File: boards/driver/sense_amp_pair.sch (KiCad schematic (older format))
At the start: 15 parts, among them T1 1:1, T2 1:1, U2 SN7524

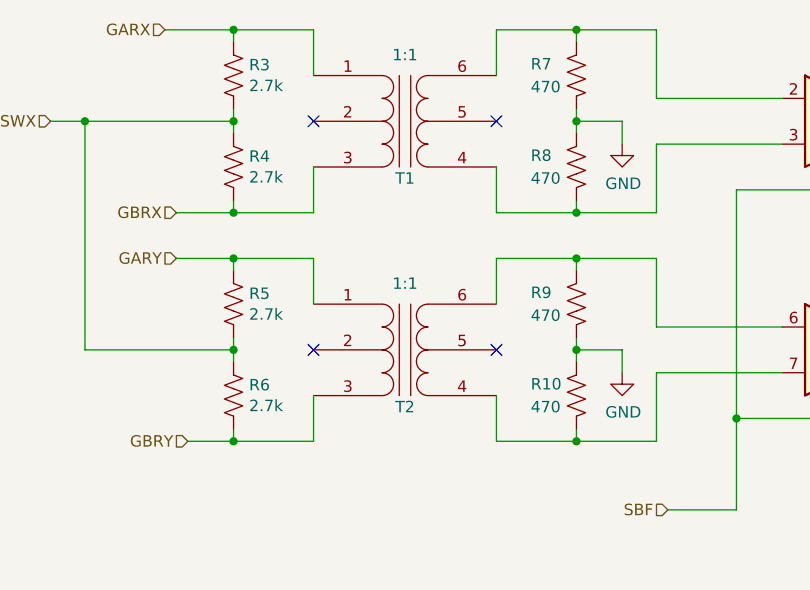
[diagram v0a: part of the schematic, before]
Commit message: Driver board: integrated DIN 41612 backplane connector, and made a dedicated parity inhibit sheet with a different set resistor value.
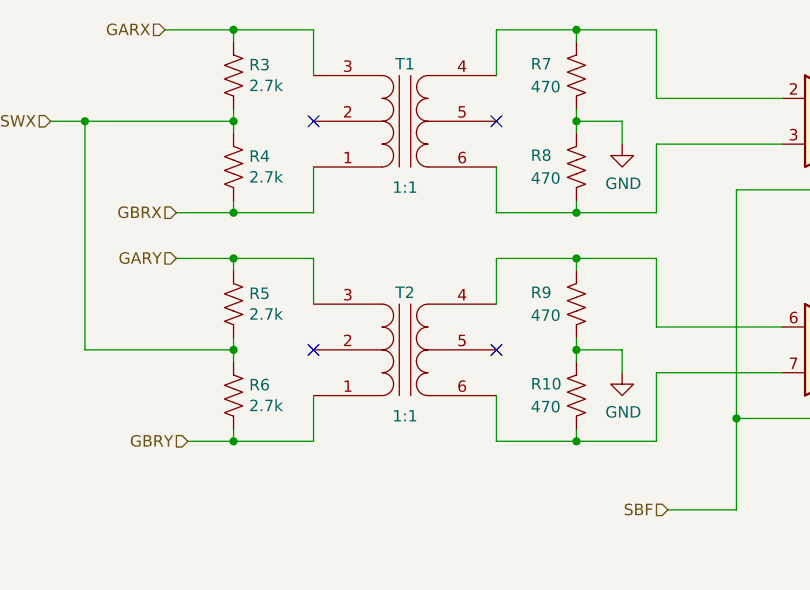
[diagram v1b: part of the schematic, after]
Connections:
- net GARX: now also T1.3 (P2); no longer T1.1 (P1)
- net GARY: now also T2.3 (P2); no longer T2.1 (P1)
- net GBRX: now also T1.1 (P1); no longer T1.3 (P2)
- net GBRY: now also T2.1 (P1); no longer T2.3 (P2)
- net at R7.1, U2.2: now also T1.4 (S2); no longer T1.6 (S1)
- net at R8.2, U2.3: now also T1.6 (S1); no longer T1.4 (S2)
- net at R9.1, U2.6: now also T2.4 (S2); no longer T2.6 (S1)
- net at R10.2, U2.7: now also T2.6 (S1); no longer T2.4 (S2)
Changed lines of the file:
@@
 F 3 "~" H 3650 2050 50  0001 C CNN
 	1    3650 2050
-	1    0    0    -1
+	1    0    0    1
 $EndComp
 NoConn ~ 3250 2050
@@
 F 3 "~" H 3650 3050 50  0001 C CNN
 	1    3650 3050
-	1    0    0    -1
+	1    0    0    1
 $EndComp
 NoConn ~ 3250 3050

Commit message: Driver: incorporated some power LEDs
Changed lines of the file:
@@
 AR Path="/61EC7443/638F119D/6358F0BC" Ref="R51"  Part="1"
 AR Path="/61EC7443/638F11C1/6358F0BC" Ref="R59"  Part="1"
-F 0 "R3" H 2968 1896 50  0000 L CNN
+F 0 "R59" H 2968 1896 50  0000 L CNN
 F 1 "2.7k" H 2968 1805 50  0000 L CNN
 F 2 "Resistor_SMD:R_0603_1608Metric" V 2940 1840 50  0001 C CNN
@@
 AR Path="/61EC7443/638F119D/6358F0C2" Ref="R52"  Part="1"
 AR Path="/61EC7443/638F11C1/6358F0C2" Ref="R60"  Part="1"
-F 0 "R4" H 2968 2296 50  0000 L CNN
+F 0 "R60" H 2968 2296 50  0000 L CNN
 F 1 "2.7k" H 2968 2205 50  0000 L CNN
 F 2 "Resistor_SMD:R_0603_1608Metric" V 2940 2240 50  0001 C CNN
@@
 AR Path="/61EC7443/638F119D/6358F0D6" Ref="R55"  Part="1"
 AR Path="/61EC7443/638F11C1/6358F0D6" Ref="R63"  Part="1"
-F 0 "R7" H 4600 1900 50  0000 R CNN
+F 0 "R63" H 4600 1900 50  0000 R CNN
 F 1 "470" H 4600 1800 50  0000 R CNN
 F 2 "Resistor_SMD:R_0603_1608Metric" V 4440 1840 50  0001 C CNN
@@
 AR Path="/61EC7443/638F119D/6358F0DC" Ref="R56"  Part="1"
 AR Path="/61EC7443/638F11C1/6358F0DC" Ref="R64"  Part="1"
-F 0 "R8" H 4600 2300 50  0000 R CNN
+F 0 "R64" H 4600 2300 50  0000 R CNN
 F 1 "470" H 4600 2200 50  0000 R CNN
 F 2 "Resistor_SMD:R_0603_1608Metric" V 4440 2240 50  0001 C CNN
@@
 AR Path="/61EC7443/638F119D/6358F0F0" Ref="#PWR043"  Part="1"
 AR Path="/61EC7443/638F11C1/6358F0F0" Ref="#PWR049"  Part="1"
-F 0 "#PWR07" H 4600 1900 50  0001 C CNN
+F 0 "#PWR049" H 4600 1900 50  0001 C CNN
 F 1 "GND" H 4605 1977 50  0000 C CNN
 F 2 "" H 4600 2150 50  0001 C CNN
@@
 AR Path="/61EC7443/638F119D/6358F0F7" Ref="U8"  Part="1"
 AR Path="/61EC7443/638F11C1/6358F0F7" Ref="U9"  Part="1"
-F 0 "U2" H 5600 2417 50  0000 C CNN
+F 0 "U9" H 5600 2417 50  0000 C CNN
 F 1 "SN7524" H 5600 2326 50  0000 C CNN
 F 2 "Package_DIP:DIP-16_W7.62mm_Socket" H 5600 2050 50  0001 C CNN
@@
 AR Path="/61EC7443/638F119D/6358F101" Ref="T13"  Part="1"
 AR Path="/61EC7443/638F11C1/6358F101" Ref="T15"  Part="1"
-F 0 "T1" H 3650 1800 50  0000 C CNN
+F 0 "T15" H 3650 1800 50  0000 C CNN
 F 1 "1:1" H 3650 2340 50  0000 C CNN
 F 2 "lachesis:Transformer_Murata_786J" H 3650 2050 50  0001 C CNN
@@
 AR Path="/61EC7443/638F119D/6358F10F" Ref="R53"  Part="1"
 AR Path="/61EC7443/638F11C1/6358F10F" Ref="R61"  Part="1"
-F 0 "R5" H 2968 2896 50  0000 L CNN
+F 0 "R61" H 2968 2896 50  0000 L CNN
 F 1 "2.7k" H 2968 2805 50  0000 L CNN
 F 2 "Resistor_SMD:R_0603_1608Metric" V 2940 2840 50  0001 C CNN
@@
 AR Path="/61EC7443/638F119D/6358F115" Ref="R54"  Part="1"
 AR Path="/61EC7443/638F11C1/6358F115" Ref="R62"  Part="1"
-F 0 "R6" H 2968 3296 50  0000 L CNN
+F 0 "R62" H 2968 3296 50  0000 L CNN
 F 1 "2.7k" H 2968 3205 50  0000 L CNN
 F 2 "Resistor_SMD:R_0603_1608Metric" V 2940 3240 50  0001 C CNN
@@
 AR Path="/61EC7443/638F119D/6358F125" Ref="R57"  Part="1"
 AR Path="/61EC7443/638F11C1/6358F125" Ref="R65"  Part="1"
-F 0 "R9" H 4600 2900 50  0000 R CNN
+F 0 "R65" H 4600 2900 50  0000 R CNN
 F 1 "470" H 4600 2800 50  0000 R CNN
 F 2 "Resistor_SMD:R_0603_1608Metric" V 4440 2840 50  0001 C CNN
@@
 AR Path="/61EC7443/638F119D/6358F12B" Ref="R58"  Part="1"
 AR Path="/61EC7443/638F11C1/6358F12B" Ref="R66"  Part="1"
-F 0 "R10" H 4600 3300 50  0000 R CNN
+F 0 "R66" H 4600 3300 50  0000 R CNN
 F 1 "470" H 4600 3200 50  0000 R CNN
 F 2 "Resistor_SMD:R_0603_1608Metric" V 4440 3240 50  0001 C CNN
@@
 AR Path="/61EC7443/638F119D/6358F13F" Ref="#PWR044"  Part="1"
 AR Path="/61EC7443/638F11C1/6358F13F" Ref="#PWR050"  Part="1"
-F 0 "#PWR08" H 4600 2900 50  0001 C CNN
+F 0 "#PWR050" H 4600 2900 50  0001 C CNN
 F 1 "GND" H 4605 2977 50  0000 C CNN
 F 2 "" H 4600 3150 50  0001 C CNN
@@
 AR Path="/61EC7443/638F119D/6358F146" Ref="U8"  Part="2"
 AR Path="/61EC7443/638F11C1/6358F146" Ref="U9"  Part="2"
-F 0 "U2" H 5600 3417 50  0000 C CNN
+F 0 "U9" H 5600 3417 50  0000 C CNN
 F 1 "SN7524" H 5600 3326 50  0000 C CNN
 F 2 "Package_DIP:DIP-16_W7.62mm_Socket" H 5600 3050 50  0001 C CNN
@@
 AR Path="/61EC7443/638F119D/6358F150" Ref="T14"  Part="1"
 AR Path="/61EC7443/638F11C1/6358F150" Ref="T16"  Part="1"
-F 0 "T2" H 3650 2800 50  0000 C CNN
+F 0 "T16" H 3650 2800 50  0000 C CNN
 F 1 "1:1" H 3650 3340 50  0000 C CNN
 F 2 "lachesis:Transformer_Murata_786J" H 3650 3050 50  0001 C CNN
@@
 AR Path="/61EC7443/638F119D/6359BB32" Ref="U8"  Part="4"
 AR Path="/61EC7443/638F11C1/6359BB32" Ref="U9"  Part="4"
-F 0 "U2" H 8050 3050 50  0000 L CNN
+F 0 "U9" H 8050 3050 50  0000 L CNN
 F 1 "SN7524" H 8050 2950 50  0000 L CNN
 F 2 "Package_DIP:DIP-16_W7.62mm_Socket" H 8100 3350 50  0001 C CNN
@@
 AR Path="/61EC7443/638F119D/6359BB38" Ref="#PWR048"  Part="1"
 AR Path="/61EC7443/638F11C1/6359BB38" Ref="#PWR054"  Part="1"
-F 0 "#PWR012" H 8550 3300 50  0001 C CNN
+F 0 "#PWR054" H 8550 3300 50  0001 C CNN
 F 1 "GND" H 8555 3377 50  0000 C CNN
 F 2 "" H 8550 3550 50  0001 C CNN
@@
 AR Path="/61EC7443/638F119D/6359BB40" Ref="C29"  Part="1"
 AR Path="/61EC7443/638F11C1/6359BB40" Ref="C33"  Part="1"
-F 0 "C5" H 8459 3304 50  0000 R CNN
+F 0 "C33" H 8459 3304 50  0000 R CNN
 F 1 "100pF" H 8459 3395 50  0000 R CNN
 F 2 "Capacitor_SMD:C_0603_1608Metric" H 8550 3350 50  0001 C CNN
@@
 AR Path="/61EC7443/638F119D/635A5721" Ref="C30"  Part="1"
 AR Path="/61EC7443/638F11C1/635A5721" Ref="C34"  Part="1"
-F 0 "C6" H 8808 3154 50  0000 R CNN
+F 0 "C34" H 8808 3154 50  0000 R CNN
 F 1 "0.1uF" H 8808 3245 50  0000 R CNN
 F 2 "Capacitor_SMD:C_0603_1608Metric" H 8900 3200 50  0001 C CNN
@@
 AR Path="/61EC7443/638F119D/635A572B" Ref="C31"  Part="1"
 AR Path="/61EC7443/638F11C1/635A572B" Ref="C35"  Part="1"
-F 0 "C7" H 8808 3654 50  0000 R CNN
+F 0 "C35" H 8808 3654 50  0000 R CNN
 F 1 "0.1uF" H 8808 3745 50  0000 R CNN
 F 2 "Capacitor_SMD:C_0603_1608Metric" H 8900 3700 50  0001 C CNN
@@
 AR Path="/61EC7443/638F119D/635B04D5" Ref="U8"  Part="3"
 AR Path="/61EC7443/638F11C1/635B04D5" Ref="U9"  Part="3"
-F 0 "U2" H 5750 4350 50  0000 C CNN
+F 0 "U9" H 5750 4350 50  0000 C CNN
 F 1 "SN7524" H 5700 4250 50  0000 C CNN
 F 2 "Package_DIP:DIP-16_W7.62mm_Socket" H 5550 4450 50  0001 C CNN
@@
 AR Path="/61EC7443/638F119D/635B04DD" Ref="C28"  Part="1"
 AR Path="/61EC7443/638F11C1/635B04DD" Ref="C32"  Part="1"
-F 0 "C4" H 5009 4404 50  0000 R CNN
+F 0 "C32" H 5009 4404 50  0000 R CNN
 F 1 "10nF" H 5009 4495 50  0000 R CNN
 F 2 "Capacitor_SMD:C_0603_1608Metric" H 5100 4450 50  0001 C CNN
@@
 AR Path="/61EC7443/638F119D/635B04EA" Ref="#PWR045"  Part="1"
 AR Path="/61EC7443/638F11C1/635B04EA" Ref="#PWR051"  Part="1"
-F 0 "#PWR09" H 4750 4400 50  0001 C CNN
+F 0 "#PWR051" H 4750 4400 50  0001 C CNN
 F 1 "GND" H 4755 4477 50  0000 C CNN
 F 2 "" H 4750 4650 50  0001 C CNN
@@
 AR Path="/61EC7443/638F119D/635E31A4" Ref="#PWR046"  Part="1"
 AR Path="/61EC7443/638F11C1/635E31A4" Ref="#PWR052"  Part="1"
-F 0 "#PWR010" H 8000 2700 50  0001 C CNN
+F 0 "#PWR052" H 8000 2700 50  0001 C CNN
 F 1 "+5V" H 8015 3023 50  0000 C CNN
 F 2 "" H 8000 2850 50  0001 C CNN
@@
 AR Path="/61EC7443/638F119D/635F8271" Ref="#PWR047"  Part="1"
 AR Path="/61EC7443/638F11C1/635F8271" Ref="#PWR053"  Part="1"
-F 0 "#PWR011" H 8000 4050 50  0001 C CNN
+F 0 "#PWR053" H 8000 4050 50  0001 C CNN
 F 1 "-5V" H 8015 4123 50  0000 C CNN
 F 2 "" H 8000 3950 50  0001 C CNN

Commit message: Driver board: largely fleshed out part selection
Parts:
- C4: Digikey (none) -> https://www.digikey.com/en/products/detail/samsung-electro-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; Part Number (none) -> CL10B103KC8NNNC; Rating (none) -> 100V; Tolerance (none) -> 10%
- C5: Digikey (none) -> https://www.digikey.com/en/products/detail/samsung-electro-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; Part Number (none) -> CL10B101KB8NFNC; Rating (none) -> 50V; Tolerance (none) -> 10%
- T1, T2: Digikey (none) -> https://www.digikey.com/en/products/detail/murata-power-sol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; Part Number (none) -> 78615/1JC
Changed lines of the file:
@@
 $Descr A4 11693 8268
 encoding utf-8
-Sheet 4 64
+Sheet 8 64
 Title ""
 Date ""
@@
 AR Path="/61EC7443/638F119D/6358F0BC" Ref="R51"  Part="1"
 AR Path="/61EC7443/638F11C1/6358F0BC" Ref="R59"  Part="1"
-F 0 "R59" H 2968 1896 50  0000 L CNN
+F 0 "R35" H 2968 1896 50  0000 L CNN
 F 1 "2.7k" H 2968 1805 50  0000 L CNN
 F 2 "Resistor_SMD:R_0603_1608Metric" V 2940 1840 50  0001 C CNN
@@
 AR Path="/61EC7443/638F119D/6358F0C2" Ref="R52"  Part="1"
 AR Path="/61EC7443/638F11C1/6358F0C2" Ref="R60"  Part="1"
-F 0 "R60" H 2968 2296 50  0000 L CNN
+F 0 "R36" H 2968 2296 50  0000 L CNN
 F 1 "2.7k" H 2968 2205 50  0000 L CNN
 F 2 "Resistor_SMD:R_0603_1608Metric" V 2940 2240 50  0001 C CNN
@@
 AR Path="/61EC7443/638F119D/6358F0D6" Ref="R55"  Part="1"
 AR Path="/61EC7443/638F11C1/6358F0D6" Ref="R63"  Part="1"
-F 0 "R63" H 4600 1900 50  0000 R CNN
+F 0 "R39" H 4600 1900 50  0000 R CNN
 F 1 "470" H 4600 1800 50  0000 R CNN
 F 2 "Resistor_SMD:R_0603_1608Metric" V 4440 1840 50  0001 C CNN
@@
 AR Path="/61EC7443/638F119D/6358F0DC" Ref="R56"  Part="1"
 AR Path="/61EC7443/638F11C1/6358F0DC" Ref="R64"  Part="1"
-F 0 "R64" H 4600 2300 50  0000 R CNN
+F 0 "R40" H 4600 2300 50  0000 R CNN
 F 1 "470" H 4600 2200 50  0000 R CNN
 F 2 "Resistor_SMD:R_0603_1608Metric" V 4440 2240 50  0001 C CNN
@@
 AR Path="/61EC7443/638F119D/6358F0F7" Ref="U8"  Part="1"
 AR Path="/61EC7443/638F11C1/6358F0F7" Ref="U9"  Part="1"
-F 0 "U9" H 5600 2417 50  0000 C CNN
+F 0 "U6" H 5600 2417 50  0000 C CNN
 F 1 "SN7524" H 5600 2326 50  0000 C CNN
 F 2 "Package_DIP:DIP-16_W7.62mm_Socket" H 5600 2050 50  0001 C CNN
@@
 AR Path="/61EC7443/638F119D/6358F101" Ref="T13"  Part="1"
 AR Path="/61EC7443/638F11C1/6358F101" Ref="T15"  Part="1"
-F 0 "T15" H 3650 1800 50  0000 C CNN
+F 0 "T9" H 3650 1800 50  0000 C CNN
 F 1 "1:1" H 3650 2340 50  0000 C CNN
 F 2 "lachesis:Transformer_Murata_786J" H 3650 2050 50  0001 C CNN
 F 3 "~" H 3650 2050 50  0001 C CNN
+F 4 "https://www.digikey.com/en/products/detail/murata-power-solutions-inc/78615-1JC/5798694" H 3650 2050 50  0001 C CNN "Digikey"
+F 5 "78615/1JC" H 3650 2050 50  0001 C CNN "Part Number"
 	1    3650 2050
 	1    0    0    1
@@
 AR Path="/61EC7443/638F119D/6358F10F" Ref="R53"  Part="1"
 AR Path="/61EC7443/638F11C1/6358F10F" Ref="R61"  Part="1"
-F 0 "R61" H 2968 2896 50  0000 L CNN
+F 0 "R37" H 2968 2896 50  0000 L CNN
 F 1 "2.7k" H 2968 2805 50  0000 L CNN
 F 2 "Resistor_SMD:R_0603_1608Metric" V 2940 2840 50  0001 C CNN
@@
 AR Path="/61EC7443/638F119D/6358F115" Ref="R54"  Part="1"
 AR Path="/61EC7443/638F11C1/6358F115" Ref="R62"  Part="1"
-F 0 "R62" H 2968 3296 50  0000 L CNN
+F 0 "R38" H 2968 3296 50  0000 L CNN
 F 1 "2.7k" H 2968 3205 50  0000 L CNN
 F 2 "Resistor_SMD:R_0603_1608Metric" V 2940 3240 50  0001 C CNN
@@
 AR Path="/61EC7443/638F119D/6358F125" Ref="R57"  Part="1"
 AR Path="/61EC7443/638F11C1/6358F125" Ref="R65"  Part="1"
-F 0 "R65" H 4600 2900 50  0000 R CNN
+F 0 "R41" H 4600 2900 50  0000 R CNN
 F 1 "470" H 4600 2800 50  0000 R CNN
 F 2 "Resistor_SMD:R_0603_1608Metric" V 4440 2840 50  0001 C CNN
@@
 AR Path="/61EC7443/638F119D/6358F12B" Ref="R58"  Part="1"
 AR Path="/61EC7443/638F11C1/6358F12B" Ref="R66"  Part="1"
-F 0 "R66" H 4600 3300 50  0000 R CNN
+F 0 "R42" H 4600 3300 50  0000 R CNN
 F 1 "470" H 4600 3200 50  0000 R CNN
 F 2 "Resistor_SMD:R_0603_1608Metric" V 4440 3240 50  0001 C CNN
@@
 AR Path="/61EC7443/638F119D/6358F146" Ref="U8"  Part="2"
 AR Path="/61EC7443/638F11C1/6358F146" Ref="U9"  Part="2"
-F 0 "U9" H 5600 3417 50  0000 C CNN
+F 0 "U6" H 5600 3417 50  0000 C CNN
 F 1 "SN7524" H 5600 3326 50  0000 C CNN
 F 2 "Package_DIP:DIP-16_W7.62mm_Socket" H 5600 3050 50  0001 C CNN
@@
 AR Path="/61EC7443/638F119D/6358F150" Ref="T14"  Part="1"
 AR Path="/61EC7443/638F11C1/6358F150" Ref="T16"  Part="1"
-F 0 "T16" H 3650 2800 50  0000 C CNN
+F 0 "T10" H 3650 2800 50  0000 C CNN
 F 1 "1:1" H 3650 3340 50  0000 C CNN
 F 2 "lachesis:Transformer_Murata_786J" H 3650 3050 50  0001 C CNN
 F 3 "~" H 3650 3050 50  0001 C CNN
+F 4 "https://www.digikey.com/en/products/detail/murata-power-solutions-inc/78615-1JC/5798694" H 3650 3050 50  0001 C CNN "Digikey"
+F 5 "78615/1JC" H 3650 3050 50  0001 C CNN "Part Number"
 	1    3650 3050
 	1    0    0    1
@@
 AR Path="/61EC7443/638F119D/6359BB32" Ref="U8"  Part="4"
 AR Path="/61EC7443/638F11C1/6359BB32" Ref="U9"  Part="4"
-F 0 "U9" H 8050 3050 50  0000 L CNN
+F 0 "U6" H 8050 3050 50  0000 L CNN
 F 1 "SN7524" H 8050 2950 50  0000 L CNN
 F 2 "Package_DIP:DIP-16_W7.62mm_Socket" H 8100 3350 50  0001 C CNN
@@
 AR Path="/61EC7443/638F119D/6359BB40" Ref="C29"  Part="1"
 AR Path="/61EC7443/638F11C1/6359BB40" Ref="C33"  Part="1"
-F 0 "C33" H 8459 3304 50  0000 R CNN
+F 0 "C21" H 8459 3304 50  0000 R CNN
 F 1 "100pF" H 8459 3395 50  0000 R CNN
 F 2 "Capacitor_SMD:C_0603_1608Metric" H 8550 3350 50  0001 C CNN
 F 3 "~" H 8550 3350 50  0001 C CNN
+F 4 "https://www.digikey.com/en/products/detail/samsung-electro-mechanics/CL10B101KB8NFNC/3887566" H 8550 3350 50  0001 C CNN "Digikey"
+F 5 "CL10B101KB8NFNC" H 8550 3350 50  0001 C CNN "Part Number"
+F 6 "50V" H 8550 3350 50  0001 C CNN "Rating"
+F 7 "10%" H 8550 3350 50  0001 C CNN "Tolerance"
 	1    8550 3350
 	-1   0    0    1
@@
 AR Path="/61EC7443/638F119D/635A5721" Ref="C30"  Part="1"
 AR Path="/61EC7443/638F11C1/635A5721" Ref="C34"  Part="1"
-F 0 "C34" H 8808 3154 50  0000 R CNN
+F 0 "C22" H 8808 3154 50  0000 R CNN
 F 1 "0.1uF" H 8808 3245 50  0000 R CNN
 F 2 "Capacitor_SMD:C_0603_1608Metric" H 8900 3200 50  0001 C CNN
@@
 AR Path="/61EC7443/638F119D/635A572B" Ref="C31"  Part="1"
 AR Path="/61EC7443/638F11C1/635A572B" Ref="C35"  Part="1"
-F 0 "C35" H 8808 3654 50  0000 R CNN
+F 0 "C23" H 8808 3654 50  0000 R CNN
 F 1 "0.1uF" H 8808 3745 50  0000 R CNN
 F 2 "Capacitor_SMD:C_0603_1608Metric" H 8900 3700 50  0001 C CNN
@@
 AR Path="/61EC7443/638F119D/635B04D5" Ref="U8"  Part="3"
 AR Path="/61EC7443/638F11C1/635B04D5" Ref="U9"  Part="3"
-F 0 "U9" H 5750 4350 50  0000 C CNN
+F 0 "U6" H 5750 4350 50  0000 C CNN
 F 1 "SN7524" H 5700 4250 50  0000 C CNN
 F 2 "Package_DIP:DIP-16_W7.62mm_Socket" H 5550 4450 50  0001 C CNN
@@
 AR Path="/61EC7443/638F119D/635B04DD" Ref="C28"  Part="1"
 AR Path="/61EC7443/638F11C1/635B04DD" Ref="C32"  Part="1"
-F 0 "C32" H 5009 4404 50  0000 R CNN
+F 0 "C20" H 5009 4404 50  0000 R CNN
 F 1 "10nF" H 5009 4495 50  0000 R CNN
 F 2 "Capacitor_SMD:C_0603_1608Metric" H 5100 4450 50  0001 C CNN
 F 3 "~" H 5100 4450 50  0001 C CNN
+F 4 "https://www.digikey.com/en/products/detail/samsung-electro-mechanics/CL10B103KC8NNNC/3886854" H 5100 4450 50  0001 C CNN "Digikey"
+F 5 "CL10B103KC8NNNC" H 5100 4450 50  0001 C CNN "Part Number"
+F 6 "100V" H 5100 4450 50  0001 C CNN "Rating"
+F 7 "10%" H 5100 4450 50  0001 C CNN "Tolerance"
 	1    5100 4450
 	1    0    0    1
